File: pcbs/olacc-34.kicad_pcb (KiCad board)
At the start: 2 copper layers, 115.8 x 94.4 mm, 22 parts

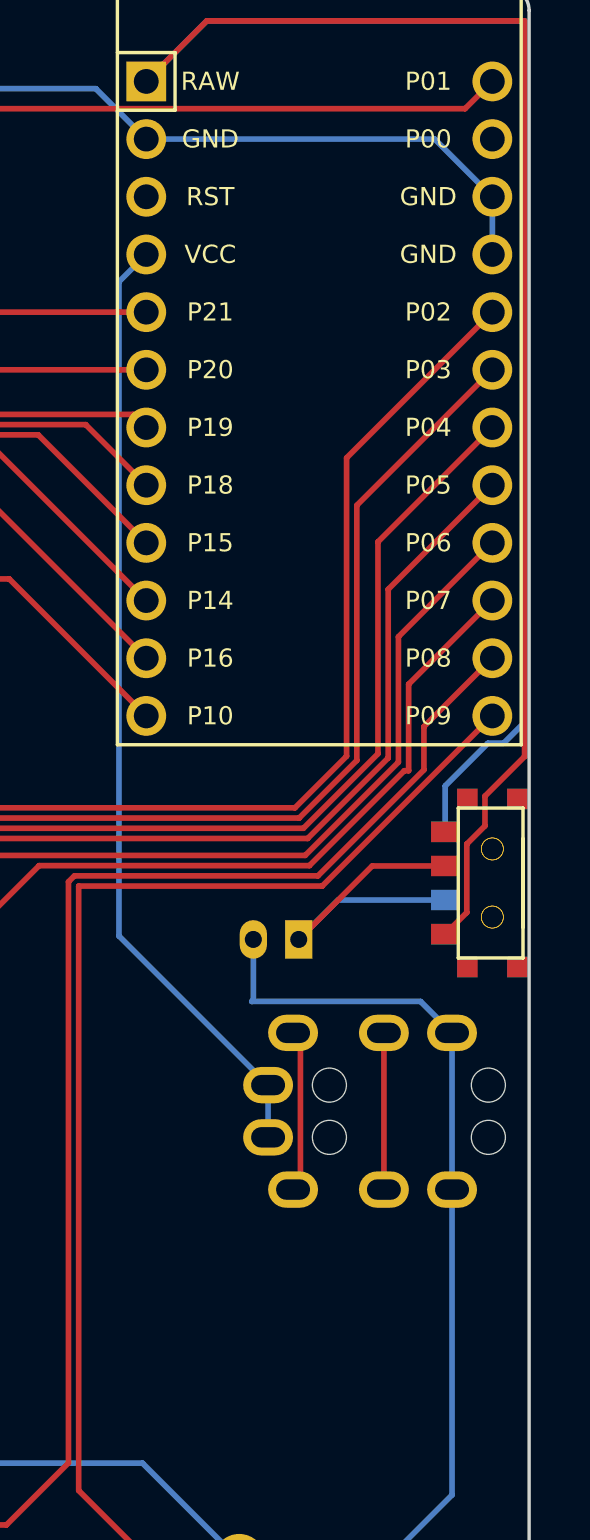
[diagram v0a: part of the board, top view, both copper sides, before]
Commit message: update pcbs with trrs and bat conns
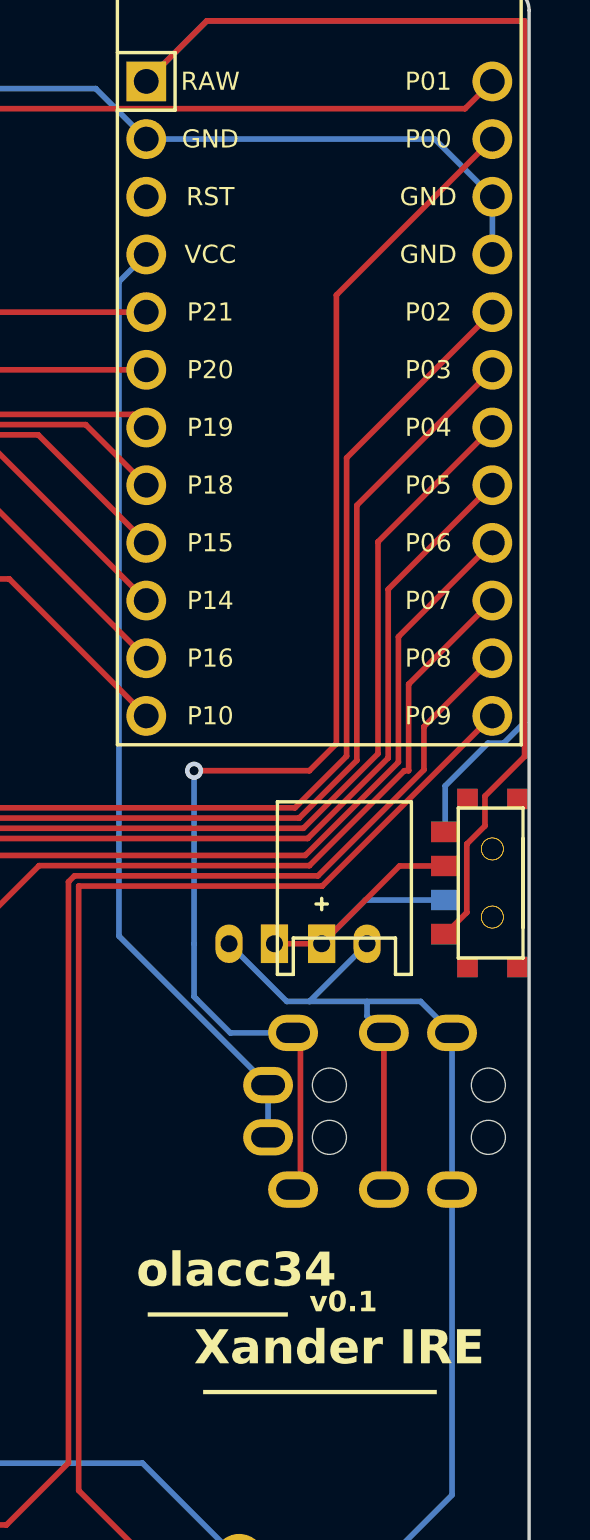
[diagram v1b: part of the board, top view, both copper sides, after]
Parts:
- added JST1: , JST_PH_S2B-PH-K_02x2.00mm_Angled, B.Cu at (98.1, -15.2)
- moved JST1 1.09 mm to (94.0, -15.2)
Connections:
- TRRS1 pad 2: P2 -> P0
- TRRS1 pad 3: P3 -> GND
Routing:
- net P0: track 0.00 -> 58.8 mm, vias 0 -> 1
- net GND: track 440.7 -> 452.2 mm
- net P2: track 7.17 -> 0.00 mm
- net P3: track 6.90 -> 0.00 mm
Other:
- board text added: "Xander IRE"
- board text added: "______"
- board text added: "__________"
- board text added: "olacc34"
- board text added: "v0.1"
